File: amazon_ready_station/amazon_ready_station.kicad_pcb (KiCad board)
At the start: 2 copper layers, 35.6 x 53.3 mm, 19 parts, among them J1 ESP 32 Left VIN GND to VP EN, J2 IR_RECVR_GND_VCC_DAT, J3 BMP180 VIN GND SCL SDA, J4 SSD1306 SDA SCL GND VCC, J5 ESP32 Right 3V3 GND to D22 D23, J6 MISC VIN GND SCL SDA, Q1 2N2219, SW1 SW_Push, SW2 SW_DIP_x01

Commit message: hackathon pcb semi-final draft
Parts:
- removed J1: ESP 32 Left VIN GND to VP EN, Connector_PinSocket_2.54mm:PinSocket_1x15_P2.54mm_Vertical
- removed J2: IR_RECVR_GND_VCC_DAT, Connector_PinSocket_2.54mm:PinSocket_1x03_P2.54mm_Vertical
- removed J3: BMP180 VIN GND SCL SDA, Connector_PinSocket_2.54mm:PinSocket_1x04_P2.54mm_Vertical
- removed J4: SSD1306 SDA SCL GND VCC, Connector_PinSocket_2.54mm:PinSocket_1x04_P2.54mm_Vertical
- removed J5: ESP32 Right 3V3 GND to D22 D23, Connector_PinSocket_2.54mm:PinSocket_1x15_P2.54mm_Vertical
- removed J6: MISC VIN GND SCL SDA, Connector_PinSocket_2.54mm:PinSocket_1x04_P2.54mm_Vertical
- removed SW1: SW_Push, Button_Switch_SMD:SW_Push_1P1T_NO_6x6mm_H9.5mm
- removed SW2: SW_DIP_x01, Button_Switch_SMD:SW_DIP_SPSTx01_Slide_6.7x4.1mm_W6.73mm_P2.54mm_LowProfile_JPin
- removed TP1, TP2, TP3, TP4, TP5, TP6: TestPoint, TestPoint:TestPoint_Pad_D2.0mm
- added BMP180: BMP180 VIN GND SCL SDA, Connector_PinSocket_2.54mm:PinSocket_1x04_P2.54mm_Vertical, F.Cu at (174.0, 109.2)
- added ESP: ESP32 Right 3V3 GND to D22 D23, Connector_PinSocket_2.54mm:PinSocket_1x15_P2.54mm_Vertical, B.Cu at (182.9, 116.8)
- added ESP: ESP 32 Left VIN GND to VP EN, Connector_PinSocket_2.54mm:PinSocket_1x15_P2.54mm_Vertical, B.Cu at (157.5, 116.8)
- added GND: TestPoint, TestPoint:TestPoint_THTPad_D2.0mm_Drill1.0mm, B.Cu at (179.1, 162.6)
- added GND: TestPoint, TestPoint:TestPoint_THTPad_D2.0mm_Drill1.0mm, B.Cu at (179.1, 111.1)
- added GND: TestPoint, TestPoint:TestPoint_THTPad_D2.0mm_Drill1.0mm, B.Cu at (156.8, 162.6)
- added I2C Device: MISC VIN GND SCL SDA, Connector_PinSocket_2.54mm:PinSocket_1x04_P2.54mm_Vertical, B.Cu at (165.7, 127.6)
- added IR Rec: IR_RECVR_DAT_VCC_GND, Connector_PinSocket_2.54mm:PinSocket_1x03_P2.54mm_Horizontal, B.Cu at (172.7, 160.7)
- added J7: BRKOUT_LEFT, Connector_PinSocket_2.54mm:PinSocket_1x15_P2.54mm_Vertical, B.Cu at (161.3, 116.8)
- added J8: BRKOUT_RIGHT, Connector_PinSocket_2.54mm:PinSocket_1x15_P2.54mm_Vertical, B.Cu at (179.1, 116.8)
- added OLED: SSD1306 GND VCC SCL SDA, Connector_PinSocket_2.54mm:PinSocket_1x04_P2.54mm_Vertical, F.Cu at (174.0, 113.0)
- added PWR: TestPoint, TestPoint:TestPoint_THTPad_D2.0mm_Drill1.0mm, B.Cu at (182.9, 111.1)
- added PWR: TestPoint, TestPoint:TestPoint_THTPad_D2.0mm_Drill1.0mm, B.Cu at (160.7, 162.6)
- added PWR: TestPoint, TestPoint:TestPoint_THTPad_D2.0mm_Drill1.0mm, B.Cu at (182.9, 162.6)
- added SW_Mode: SW_DIP_x01, Button_Switch_SMD:SW_DIP_SPSTx01_Slide_6.7x4.1mm_W6.73mm_P2.54mm_LowProfile_JPin, F.Cu at (165.7, 149.4)
- added SW_Trig: SW_Push, Button_Switch_SMD:SW_Push_1P1T_NO_6x6mm_H9.5mm, F.Cu at (173.4, 149.2)
- moved R4 58.7 mm to (175.3, 129.2)
- moved R3 55.0 mm to (175.3, 141.3)
- moved R1 48.8 mm to (166.6, 142.2), turned to 0 degrees
- moved Q1 48.2 mm to (173.7, 123.6), turned to 90 degrees
- moved R2 44.2 mm to (172.1, 136.6), turned to 90 degrees
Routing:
- net /SCL: track 0.00 -> 54.8 mm
- net /SDA: track 0.00 -> 46.7 mm, vias 0 -> 2
- net Net-(J1-Pad5): track 0.00 -> 43.3 mm
- net Net-(J1-Pad3): track 0.00 -> 41.1 mm, vias 0 -> 1
- net Net-(J2-Pad1): track 0.00 -> 31.5 mm
- net Net-(J1-Pad6): track 0.00 -> 23.0 mm
- net /GND: track 0.00 -> 11.3 mm, vias 0 -> 4
- net Net-(J5-Pad9): track 0.00 -> 3.81 mm
- net Net-(J5-Pad8): track 0.00 -> 3.81 mm
- net Net-(J5-Pad7): track 0.00 -> 3.81 mm
- net Net-(J5-Pad6): track 0.00 -> 3.81 mm
- net Net-(J5-Pad5): track 0.00 -> 3.81 mm
- net Net-(J5-Pad4): track 0.00 -> 3.81 mm
- net Net-(J5-Pad3): track 0.00 -> 3.81 mm
- net Net-(J5-Pad15): track 0.00 -> 3.81 mm
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- added copper zone on F.Cu, net /3V3
- added copper zone on B.Cu, net /5VGD
- added copper zone on F.Cu, net /5VIN
- added copper zone on B.Cu, net /GND
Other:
- board size 35.6 x 53.3 mm -> 34.3 x 68.6 mm
- rule trace_min: 0.2 -> 0.1524
- rule via_min_size: 0.4 -> 0.254
- board text added: "12"
- board text added: "13"
- board text added: "14"
- board text added: "23 22 1 3 21 19 18 5 17 16 4 2 15 GD 3V3"
- board text added: "25"
- board text added: "26"
- board text added: "27"
- board text added: "32"
- board text added: "33"
- board text added: "34"
- board text added: "35"
- board text added: "36"
- board text added: "39"
- board text added: "5VIN"
- board text added: "DAT VIN GND"
- board text added: "EN"
- board text added: "GD"
- board text added: "GND PWR"
- board text added: "Made by Analytical Mechanical Associates"
- board text added: "SCL"
- board text added: "SCL VIN GD"
- board text added: "SDA"
- board text added: "SDA SCL GD VIN"
- board text added: "VIN"
- board text added: "^^ ESP 32 USB ^^"

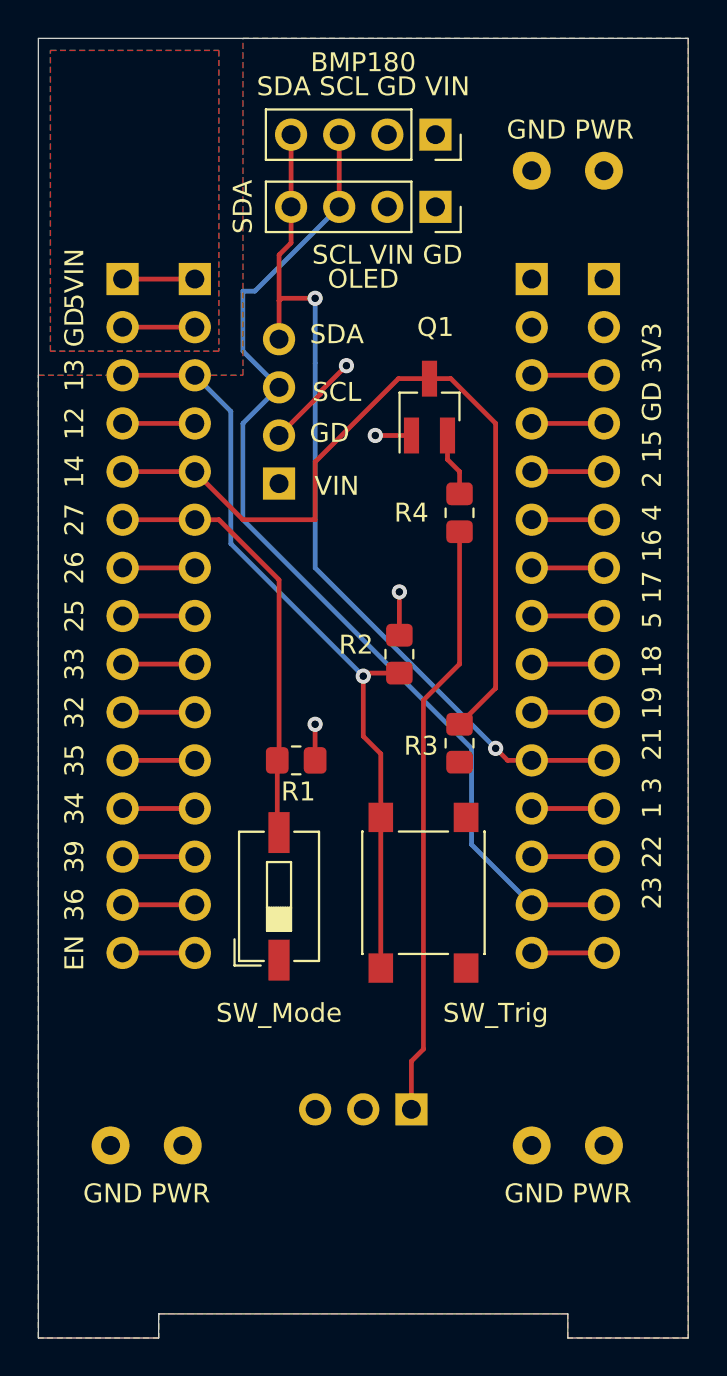
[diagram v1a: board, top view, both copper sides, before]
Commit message: chamfer edges, fix oled orientation bug
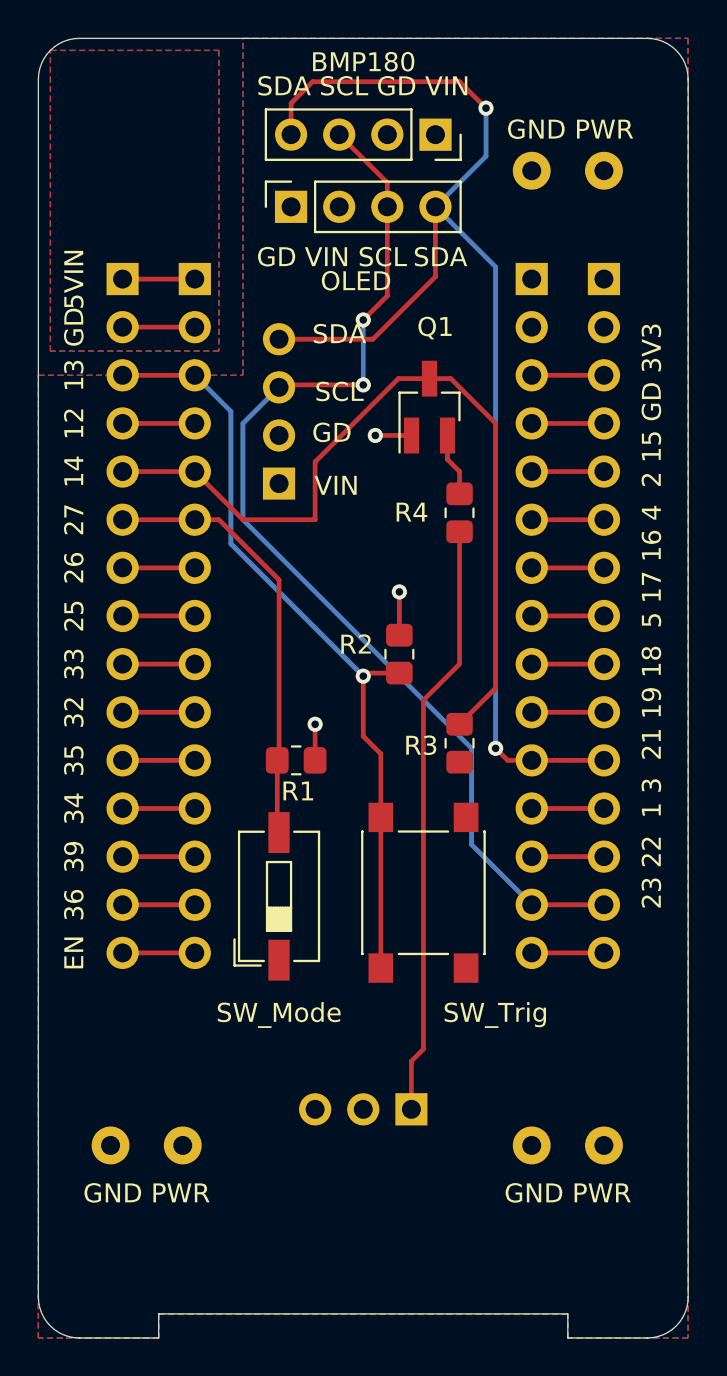
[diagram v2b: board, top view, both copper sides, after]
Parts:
- moved OLED 7.62 mm to (166.4, 113.0), turned to 90 degrees
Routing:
- net /SDA: track 46.7 -> 68.9 mm
- net /GND: track 11.3 -> 6.10 mm, vias 4 -> 3
- net /SCL: track 54.8 -> 57.5 mm, vias 0 -> 2
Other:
- outline, holes or cut-outs redrawn
- board text removed: "SCL VIN GD"

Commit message: update pcb and add time slider to virginia demo
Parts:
- removed BMP180: BMP180 VIN GND SCL SDA, Connector_PinSocket_2.54mm:PinSocket_1x04_P2.54mm_Vertical
- removed the ESP at (182.9, 116.8)
- removed GND, PWR: TestPoint, TestPoint:TestPoint_THTPad_D2.0mm_Drill1.0mm
- removed IR Rec: IR_RECVR_DAT_VCC_GND, Connector_PinSocket_2.54mm:PinSocket_1x03_P2.54mm_Horizontal
- removed SW_Mode: SW_DIP_x01, Button_Switch_SMD:SW_DIP_SPSTx01_Slide_6.7x4.1mm_W6.73mm_P2.54mm_LowProfile_JPin
- removed SW_Trig: SW_Push, Button_Switch_SMD:SW_Push_1P1T_NO_6x6mm_H9.5mm
- added 5V GD: TestPoint, amazon_ready_station:pad_right, F.Cu at (162.7, 104.8)
- added 5V GD: TestPoint, TestPoint:TestPoint_THTPad_D2.0mm_Drill1.0mm, B.Cu at (161.3, 113.0)
- added 5V GD: TestPoint, TestPoint:TestPoint_THTPad_D2.0mm_Drill1.0mm, B.Cu at (161.3, 109.7)
- added 5V IN: TestPoint, amazon_ready_station:pad_left, F.Cu at (177.7, 104.8)
- added 5V IN: TestPoint, TestPoint:TestPoint_THTPad_D2.0mm_Drill1.0mm, B.Cu at (179.1, 113.0)
- added 5V IN: TestPoint, TestPoint:TestPoint_THTPad_D2.0mm_Drill1.0mm, B.Cu at (179.1, 109.7)
- added BME280: BMP180 VIN GND SCL SDA, Connector_PinSocket_2.54mm:PinSocket_1x04_P2.54mm_Vertical, F.Cu at (174.0, 107.4)
- added IR Recv: IR_RECVR_GND_VIN_DAT, Connector_PinSocket_2.54mm:PinSocket_1x03_P2.54mm_Horizontal, F.Cu at (167.6, 157.6)
- added J5: ESP32 Right 3V3 GND to D22 D23, Connector_PinSocket_2.54mm:PinSocket_1x15_P2.54mm_Vertical, B.Cu at (182.9, 116.8)
- added Mode: SW_Push, Button_Switch_SMD:SW_Push_1P1T_NO_6x6mm_H9.5mm, F.Cu at (166.4, 149.2)
- added Trigger: SW_Push, Button_Switch_SMD:SW_Push_1P1T_NO_6x6mm_H9.5mm, F.Cu at (174.0, 149.2)
- I2C: renamed from I2C Device
- renumbered PWR to 3V3, GND to GD
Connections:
- ESP pad 1: /5VGD -> /5VIN
- ESP pad 2: /5VIN -> /5VGD
- J7 pad 1: /5VGD -> /5VIN
- J7 pad 2: /5VIN -> /5VGD
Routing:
- net /5VIN: track 3.81 -> 51.5 mm
- net /GND: track 6.10 -> 36.6 mm
- net /5VGD: track 3.81 -> 21.0 mm
- net Net-(J1-Pad6): track 23.0 -> 31.8 mm
- net /SDA: track 68.9 -> 61.3 mm, vias 2 -> 1
- net Net-(J2-Pad3): track 31.5 -> 28.5 mm
- net /SCL: track 57.5 -> 60.2 mm
- net Net-(J1-Pad3): track 41.1 -> 41.8 mm
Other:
- board size 34.3 x 68.6 mm -> 34.3 x 64.1 mm
- board text added: "23 22 1 3 21 19 18 5 17 16 4 2 15 GD"
- board text added: "3V3"
- board text added: "5V GD"
- board text added: "5V IN"
- board text added: "DAT"
- board text added: "GND 3V3"
- board text added: "Made by A. Tambe, Analytical Mechanical Associates"
- board text added: "OUT"
- board text removed: "23 22 1 3 21 19 18 5 17 16 4 2 15 GD 3V3"
- board text removed: "DAT VIN GND"
- board text removed: "GND PWR"
- board text removed: "Made by Analytical Mechanical Associates"

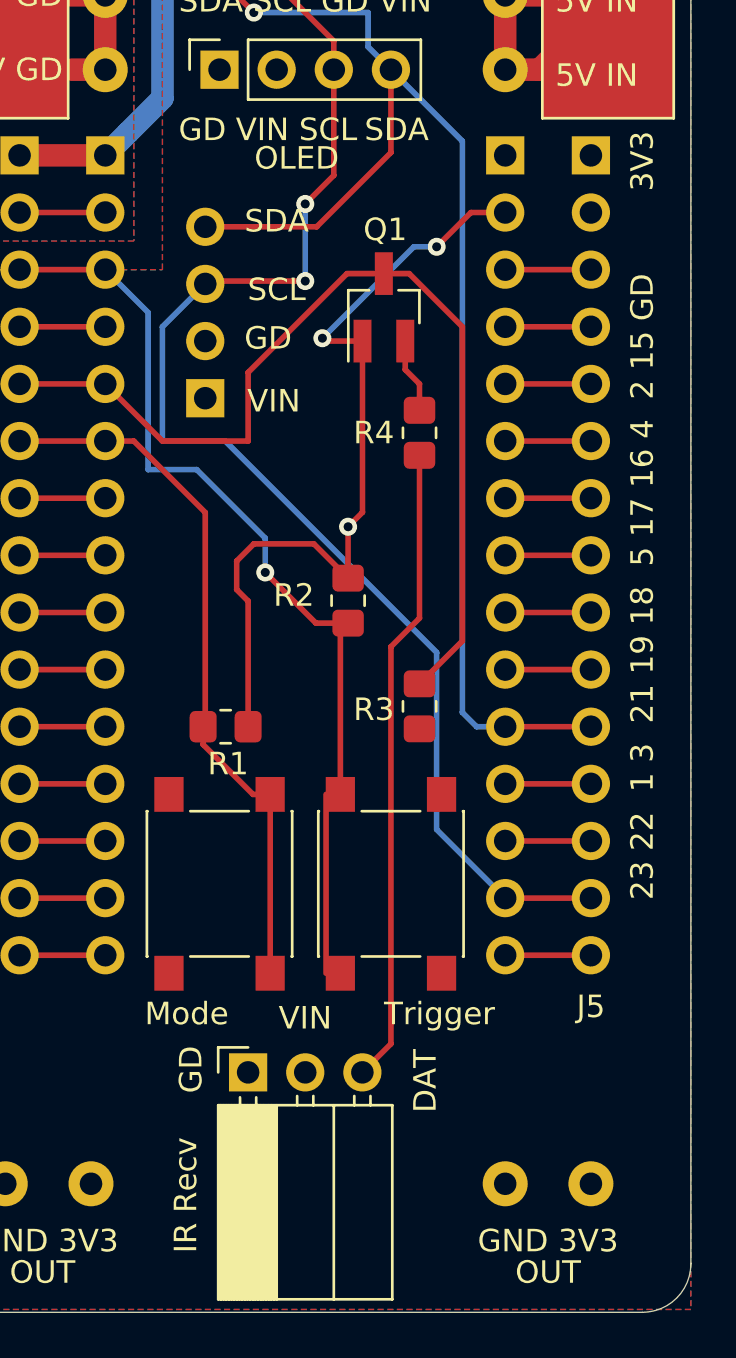
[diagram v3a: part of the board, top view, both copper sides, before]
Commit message: added artwork, edited silkscreen
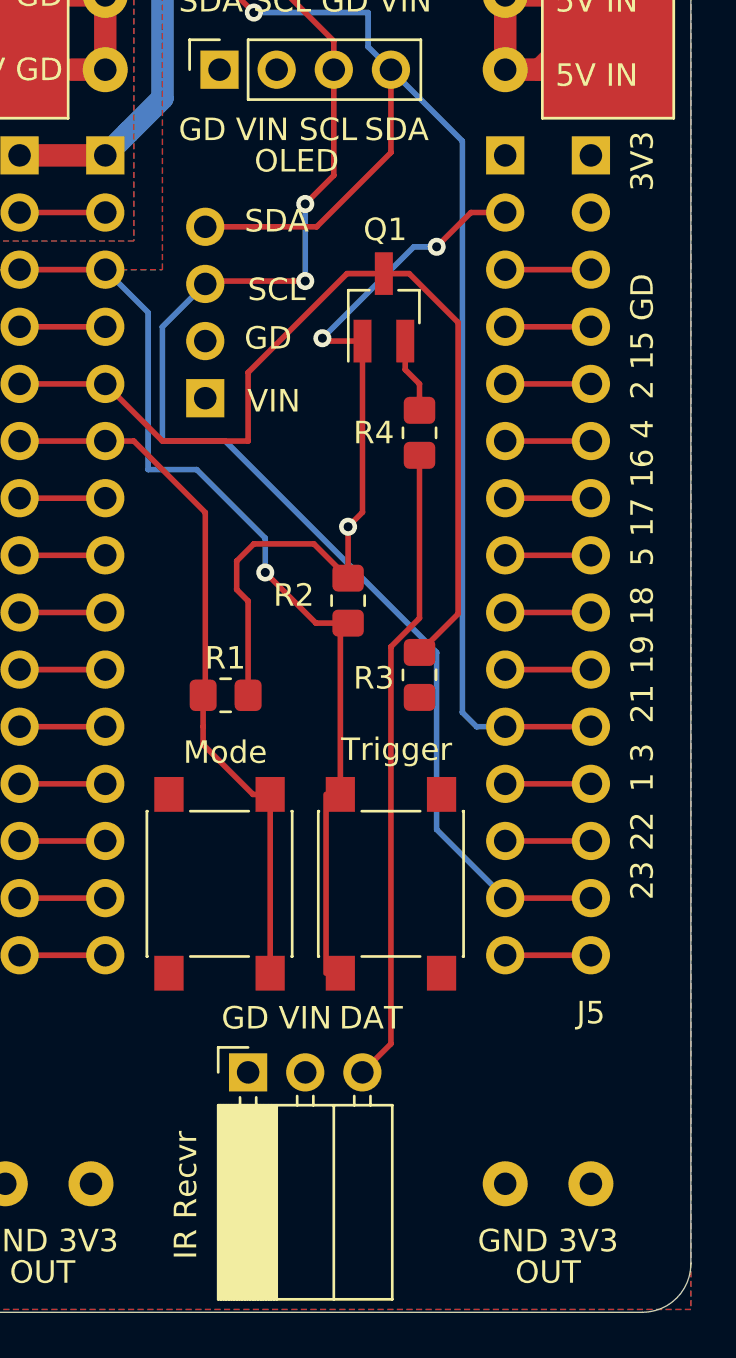
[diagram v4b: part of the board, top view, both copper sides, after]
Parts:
- added G***: LOGO, amazon_ready_station:plane_graphic, B.Cu at (169.9, 145.6)
- IR Recvr: renamed from IR Recv
- TP4, TP7: renamed from 5V GD
- TP5, TP8: renamed from 5V IN
- moved R1 1.40 mm to (166.6, 140.8)
- moved R3 1.40 mm to (175.3, 139.9)
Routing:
- net Net-(J1-Pad5): track 43.3 -> 41.7 mm
- net /GND: track 36.6 -> 35.2 mm
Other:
- board text added: "Remote Data Logger"

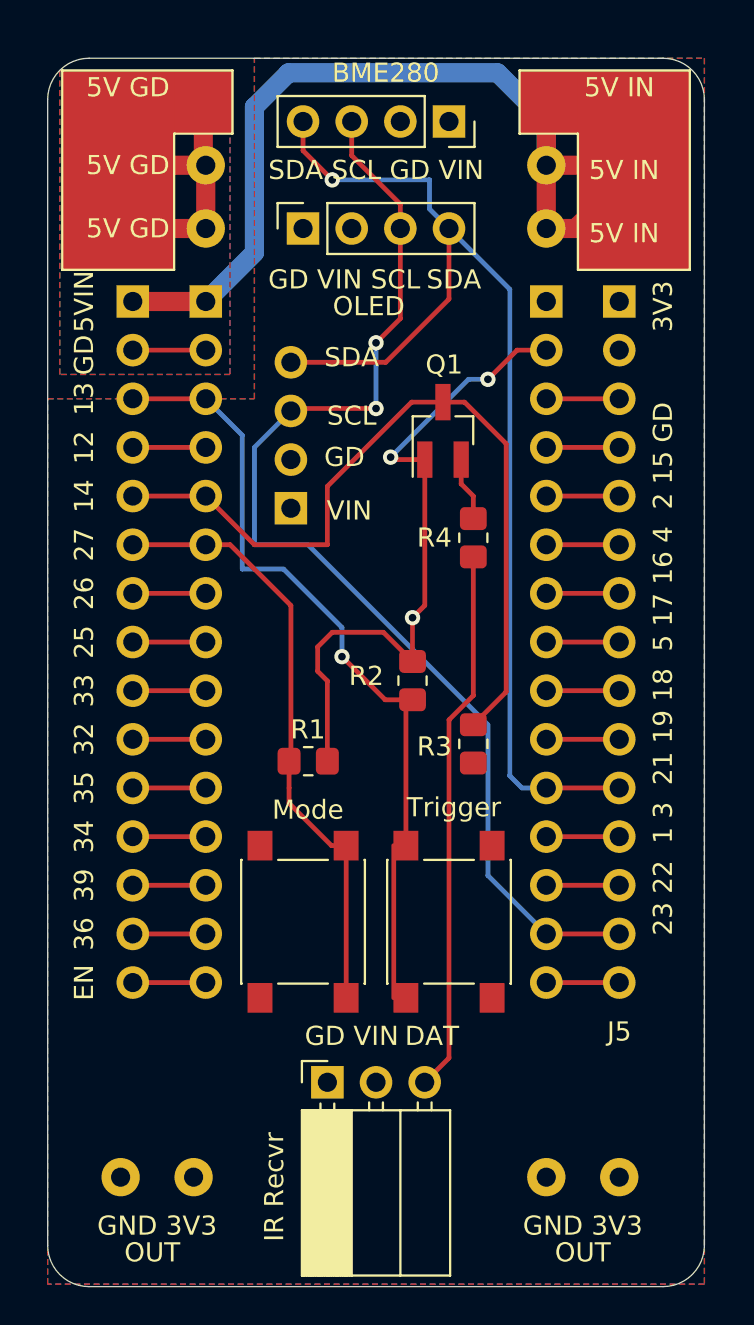
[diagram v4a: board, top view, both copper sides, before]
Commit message: added screw holes and edited Pwr In plates
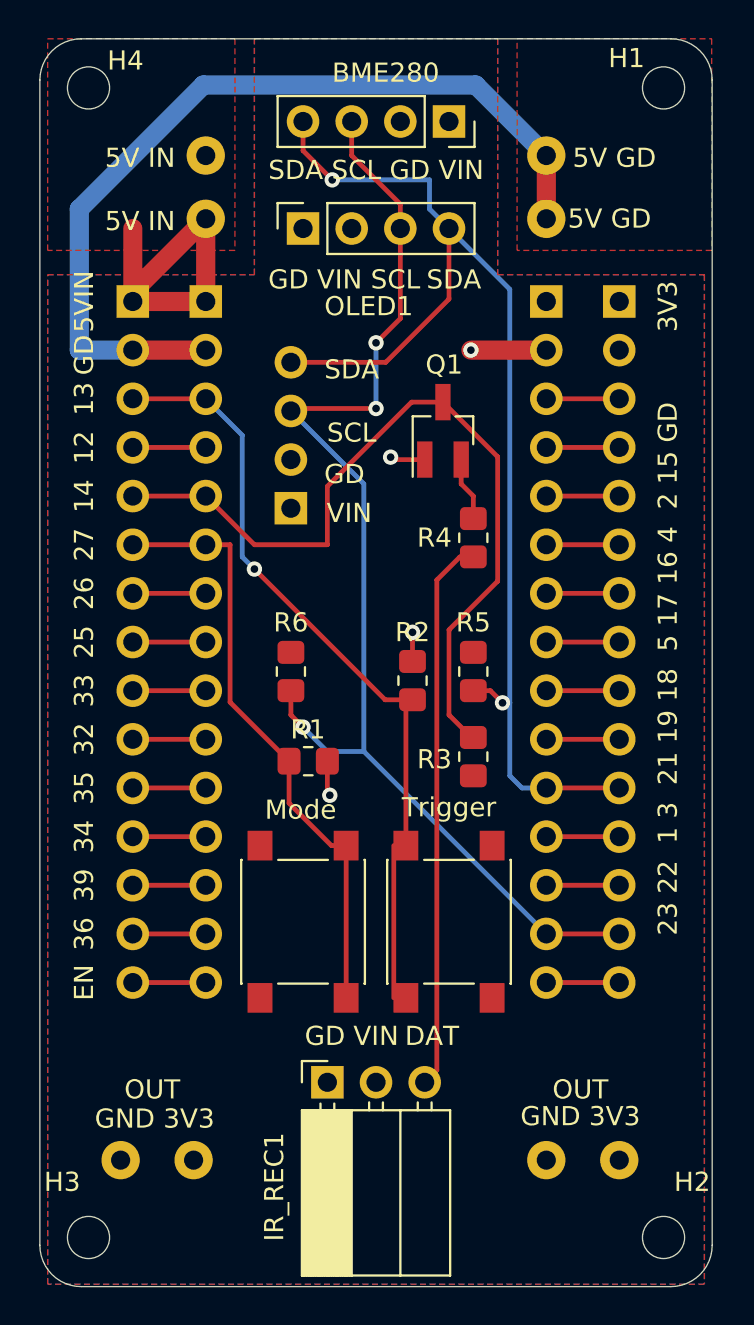
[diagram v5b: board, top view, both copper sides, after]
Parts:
- removed 3V3 (x2), GD (x2): TestPoint, TestPoint:TestPoint_THTPad_D2.0mm_Drill1.0mm
- removed 5V GD: TestPoint, amazon_ready_station:pad_right
- removed 5V IN: TestPoint, amazon_ready_station:pad_left
- added 3.3V1: TestPoint, TestPoint:TestPoint_THTPad_D2.0mm_Drill1.0mm, B.Cu at (182.9, 161.7)
- added 3.3V2: TestPoint, TestPoint:TestPoint_THTPad_D2.0mm_Drill1.0mm, B.Cu at (160.7, 161.7)
- added GND1: TestPoint, TestPoint:TestPoint_THTPad_D2.0mm_Drill1.0mm, B.Cu at (179.1, 161.7)
- added GND2: TestPoint, TestPoint:TestPoint_THTPad_D2.0mm_Drill1.0mm, B.Cu at (156.8, 161.7)
- added H1: MountingHole, MountingHole:MountingHole_2.2mm_M2, F.Cu at (185.2, 105.7)
- added H2: MountingHole, MountingHole:MountingHole_2.2mm_M2, F.Cu at (185.2, 165.7)
- added H3: MountingHole, MountingHole:MountingHole_2.2mm_M2, F.Cu at (155.2, 165.7)
- added H4: MountingHole, MountingHole:MountingHole_2.2mm_M2, F.Cu at (155.2, 105.7)
- added R5: 2400, Resistor_SMD:R_0805_2012Metric_Pad1.20x1.40mm_HandSolder, F.Cu at (175.3, 136.2)
- added R6: 2400, Resistor_SMD:R_0805_2012Metric_Pad1.20x1.40mm_HandSolder, F.Cu at (165.7, 136.2)
- IR_REC1: renamed from IR Recvr
- moved 5V_GD1 17.8 mm to (179.1, 109.2)
- moved 5V_GD2 17.8 mm to (179.1, 112.5)
- moved 5V_IN1 17.8 mm to (161.3, 109.2)
- moved 5V_IN2 17.8 mm to (161.3, 112.5)
- moved R3 0.67 mm to (175.3, 140.6)
- renumbered TP7 to 5V_GD1, TP4 to 5V_GD2, TP8 to 5V_IN1, TP5 to 5V_IN2, ESP to ESP1, J5 to ESP2, I2C to I2C1, OLED to OLED1
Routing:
- net /5VIN: track 51.5 -> 18.0 mm
- net /GND: track 35.2 -> 9.25 mm, vias 3 -> 4
- net /5VGD: track 21.0 -> 45.9 mm
- net /SCL: track 60.2 -> 62.8 mm, vias 2 -> 3
- net /SDA: track 61.3 -> 63.6 mm, vias 1 -> 2
- net Net-(ESP1-Pad3): track 41.8 -> 40.5 mm
- net Net-(ESP1-Pad5): track 41.7 -> 42.4 mm
- added copper zone on F.Cu, net /5VGD
- removed copper zone on B.Cu, net /5VGD
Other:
- board size 34.3 x 64.1 mm -> 35.1 x 65.2 mm
- board text added: "Remote Data Logger v1.4"
- board text removed: "Remote Data Logger"
